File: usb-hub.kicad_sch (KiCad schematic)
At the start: 37 parts, among them IC101 USB2517, J101 Barrel_Jack_Switch, J102 USB_C_Receptacle_USB2.0_14P, U101 USBLC6-2P6, Y101 24Mhz

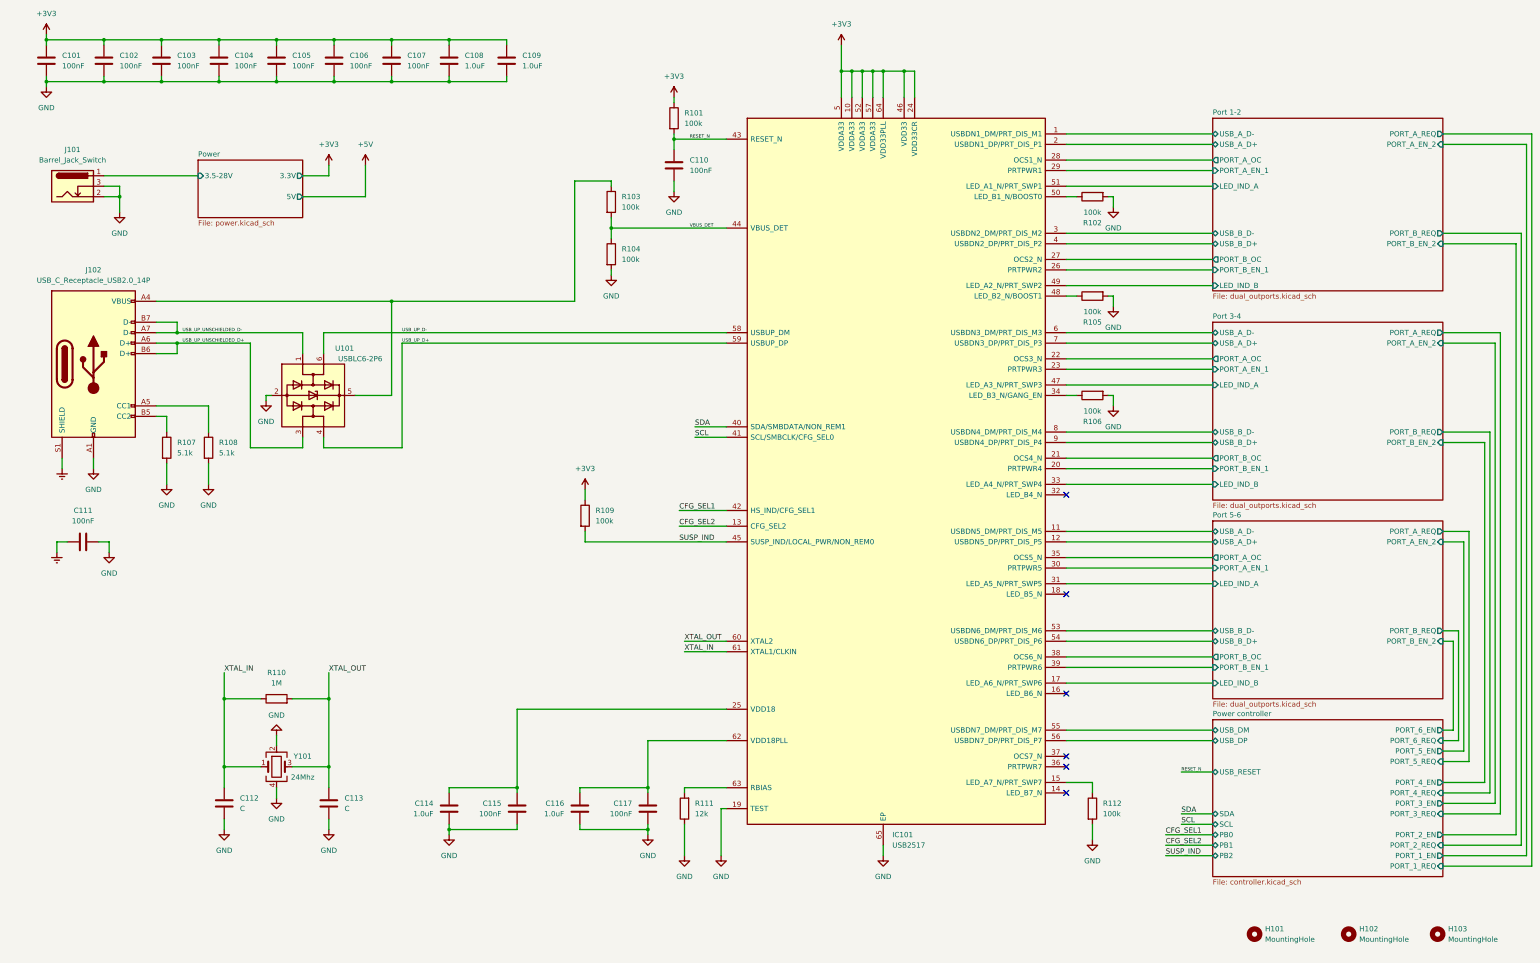
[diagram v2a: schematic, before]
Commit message: Add preliminary routing
Add routing for power paths - 3.3V, 5V and Input power

Add routing close to USB-Ports

Mising routing for main IC's and differntial pair routing
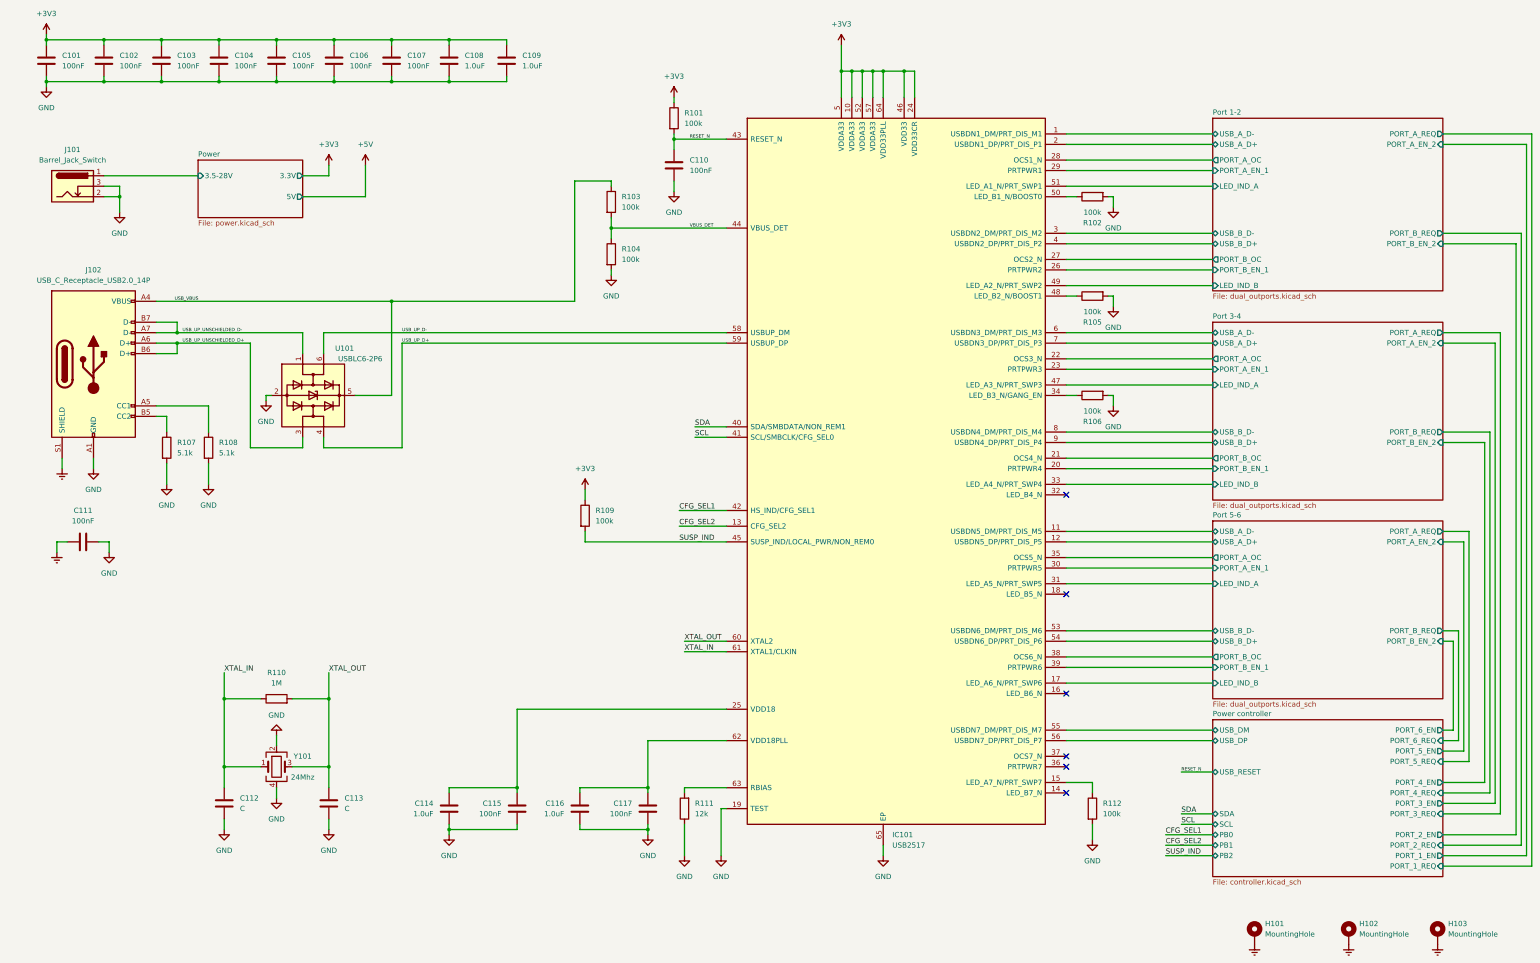
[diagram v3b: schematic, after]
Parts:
- H101, H102, H103: footprint MountingHole:MountingHole_3.2mm_M3 -> MountingHole:MountingHole_3.2mm_M3_Pad_Via; symbol Mechanical:MountingHole -> Mechanical:MountingHole_Pad; now left out of the parts list
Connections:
- net Earth: now also H101.1, H102.1, H103.1
- net USB_VBUS: now reaches J102.A4 (VBUS), J102.A9 (VBUS), J102.B4 (VBUS), J102.B9 (VBUS), R103.1, U101.5 (VBUS)
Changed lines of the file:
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@@
+    (effects (font (size 0.8 0.8)) (justify left bottom))
+  )
+  (label "USB_VBUS" (at 55.245 90.17 0) (fields_autoplaced)
     (effects (font (size 0.8 0.8)) (justify left bottom))
   )
@@
     )
   )
-  (symbol (lib_id "Mechanical:MountingHole") (at 340.36 243.84 0) (unit 1)
-    (in_bom yes) (on_board yes) (dnp no) (fields_autoplaced)
-    (property "Reference" "H102" (at 342.9 242.57 0)
-      (effects (font (size 1.27 1.27)) (justify left))
-    )
-    (property "Value" "MountingHole" (at 342.9 245.11 0)
-      (effects (font (size 1.27 1.27)) (justify left))
-    )
-    (property "Footprint" "MountingHole:MountingHole_3.2mm_M3" (at 340.36 243.84 0)
+  (symbol (lib_id "Mechanical:MountingHole_Pad") (at 340.36 243.84 0) (unit 1)
+    (in_bom no) (on_board yes) (dnp no) (fields_autoplaced)
+    (property "Reference" "H102" (at 342.9 241.3 0)
+      (effects (font (size 1.27 1.27)) (justify left))
+    )
+    (property "Value" "MountingHole" (at 342.9 243.84 0)
+      (effects (font (size 1.27 1.27)) (justify left))
+    )
+    (property "Footprint" "MountingHole:MountingHole_3.2mm_M3_Pad_Via" (at 340.36 243.84 0)
       (effects (font (size 1.27 1.27)) hide)
     )
@@
       (effects (font (size 1.27 1.27)) hide)
     )
+    (pin "1")
     (instances
       (project "usb-hub"
@@
     )
   )
-  (symbol (lib_id "Mechanical:MountingHole") (at 317.5 243.84 0) (unit 1)
-    (in_bom yes) (on_board yes) (dnp no) (fields_autoplaced)
-    (property "Reference" "H101" (at 320.04 242.57 0)
-      (effects (font (size 1.27 1.27)) (justify left))
-    )
-    (property "Value" "MountingHole" (at 320.04 245.11 0)
-      (effects (font (size 1.27 1.27)) (justify left))
-    )
-    (property "Footprint" "MountingHole:MountingHole_3.2mm_M3" (at 317.5 243.84 0)
+  (symbol (lib_id "Mechanical:MountingHole_Pad") (at 317.5 243.84 0) (unit 1)
+    (in_bom no) (on_board yes) (dnp no) (fields_autoplaced)
+    (property "Reference" "H101" (at 320.04 241.3 0)
+      (effects (font (size 1.27 1.27)) (justify left))
+    )
+    (property "Value" "MountingHole" (at 320.04 243.84 0)
+      (effects (font (size 1.27 1.27)) (justify left))
+    )
+    (property "Footprint" "MountingHole:MountingHole_3.2mm_M3_Pad_Via" (at 317.5 243.84 0)
       (effects (font (size 1.27 1.27)) hide)
     )
@@
       (effects (font (size 1.27 1.27)) hide)
     )
+    (pin "1")
     (instances
       (project "usb-hub"
@@
     )
   )
+  (symbol (lib_id "power:Earth") (at 340.36 246.38 0) (unit 1)
+    (in_bom yes) (on_board yes) (dnp no) (fields_autoplaced)
+    (property "Reference" "#PWR02" (at 340.36 252.73 0)
+      (effects (font (size 1.27 1.27)) hide)
+    )
+    (property "Value" "Earth" (at 340.36 250.19 0)
+      (effects (font (size 1.27 1.27)) hide)
+    )
+    (property "Footprint" "" (at 340.36 246.38 0)
+      (effects (font (size 1.27 1.27)) hide)
+    )
+    (property "Datasheet" "~" (at 340.36 246.38 0)
+      (effects (font (size 1.27 1.27)) hide)
+    )
+    (pin "1")
+    (instances
+      (project "usb-hub"
+        (path "/b46faf57-adcb-44f4-ac46-f905e4e8952b"
+          (reference "#PWR02") (unit 1)
+        )
+      )
+    )
+  )
   (symbol (lib_id "power:+5V") (at 101.6 57.15 0) (unit 1)
     (in_bom yes) (on_board yes) (dnp no) (fields_autoplaced)
@@
         (path "/b46faf57-adcb-44f4-ac46-f905e4e8952b"
           (reference "R103") (unit 1)
+        )
+      )
+    )
+  )
+  (symbol (lib_id "power:Earth") (at 317.5 246.38 0) (unit 1)
+    (in_bom yes) (on_board yes) (dnp no) (fields_autoplaced)
+    (property "Reference" "#PWR01" (at 317.5 252.73 0)
+      (effects (font (size 1.27 1.27)) hide)
+    )
+    (property "Value" "Earth" (at 317.5 250.19 0)
+      (effects (font (size 1.27 1.27)) hide)
+    )
+    (property "Footprint" "" (at 317.5 246.38 0)
+      (effects (font (size 1.27 1.27)) hide)
+    )
+    (property "Datasheet" "~" (at 317.5 246.38 0)
+      (effects (font (size 1.27 1.27)) hide)
+    )
+    (pin "1")
+    (instances
+      (project "usb-hub"
+        (path "/b46faf57-adcb-44f4-ac46-f905e4e8952b"
+          (reference "#PWR01") (unit 1)
         )
       )
@@
     )
   )
-  (symbol (lib_id "Mechanical:MountingHole") (at 361.95 243.84 0) (unit 1)
-    (in_bom yes) (on_board yes) (dnp no) (fields_autoplaced)
-    (property "Reference" "H103" (at 364.49 242.57 0)
-      (effects (font (size 1.27 1.27)) (justify left))
-    )
-    (property "Value" "MountingHole" (at 364.49 245.11 0)
-      (effects (font (size 1.27 1.27)) (justify left))
-    )
-    (property "Footprint" "MountingHole:MountingHole_3.2mm_M3" (at 361.95 243.84 0)
+  (symbol (lib_id "Mechanical:MountingHole_Pad") (at 361.95 243.84 0) (unit 1)
+    (in_bom no) (on_board yes) (dnp no) (fields_autoplaced)
+    (property "Reference" "H103" (at 364.49 241.3 0)
+      (effects (font (size 1.27 1.27)) (justify left))
+    )
+    (property "Value" "MountingHole" (at 364.49 243.84 0)
+      (effects (font (size 1.27 1.27)) (justify left))
+    )
+    (property "Footprint" "MountingHole:MountingHole_3.2mm_M3_Pad_Via" (at 361.95 243.84 0)
       (effects (font (size 1.27 1.27)) hide)
     )
@@
       (effects (font (size 1.27 1.27)) hide)
     )
+    (pin "1")
     (instances
       (project "usb-hub"
@@
         )
       )
+    )
+  )
+  (symbol (lib_id "power:Earth") (at 361.95 246.38 0) (unit 1)
+    (in_bom yes) (on_board yes) (dnp no) (fields_autoplaced)
+    (property "Reference" "#PWR03" (at 361.95 252.73 0)
+      (effects (font (size 1.27 1.27)) hide)
+    )
+    (property "Value" "Earth" (at 361.95 250.19 0)
+      (effects (font (size 1.27 1.27)) hide)
+    )
+    (property "Footprint" "" (at 361.95 246.38 0)
+      (effects (font (size 1.27 1.27)) hide)
+    )
+    (property "Datasheet" "~" (at 361.95 246.38 0)
+      (effects (font (size 1.27 1.27)) hide)
+    )
+    (pin "1")
+    (instances
+      (project "usb-hub"
+        (path "/b46faf57-adcb-44f4-ac46-f905e4e8952b"
+          (reference "#PWR03") (unit 1)
+        )
+      )
